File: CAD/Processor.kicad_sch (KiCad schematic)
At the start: 78 parts, among them M1 FID, M11 MOUNTING, M12 Logo_KICAD, M15 MOUNTING, M2 FID, M3 MOUNTING, M9 MOUNTING, U11 ATSAME70Q20B-ANT, X1 ECS-120-10-33B-CKM-TR

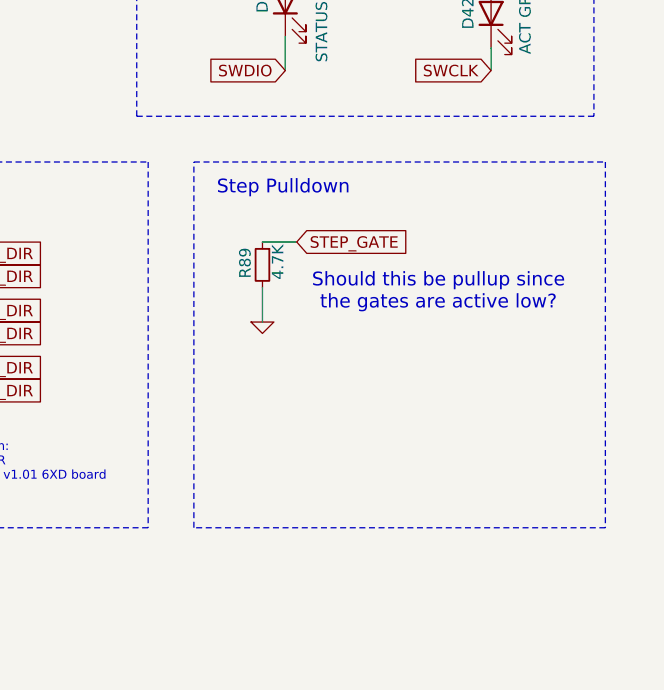
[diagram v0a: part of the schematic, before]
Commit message: Remove Step gate
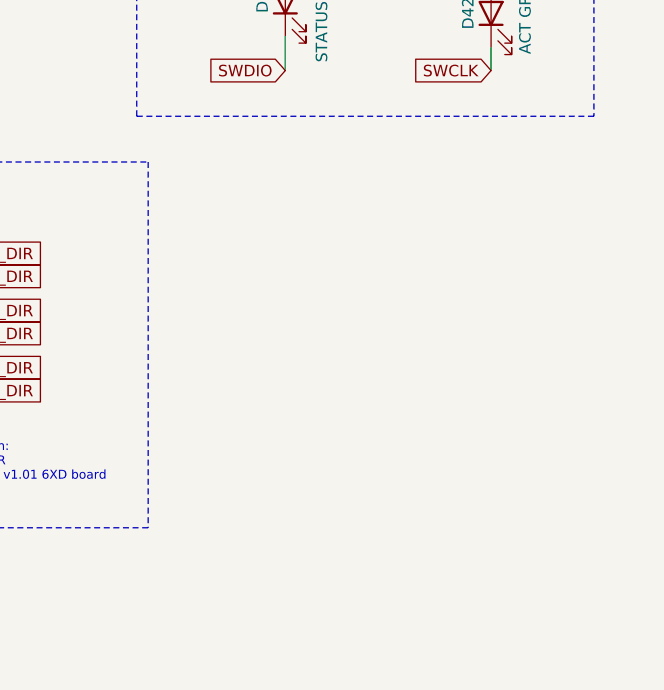
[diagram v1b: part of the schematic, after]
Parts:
- removed R89: 4.7K, Resistor_SMD:R_0402_1005Metric_Wbry, symbol Device:R_Small
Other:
- note removed: "Should this be pullup since the gates are active low?"
- note removed: "Step Pulldown"

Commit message: Pin Changes / Misc
Changing some pins around so I have a chip select
Processor Pins:
PC28 ---> PA9 (Driver_2_Step)
PC29[AFE1_AD4] ---> PB1[AFE1_AD0] (TEMP_1)
PC28 -> spi1cs1
PC29 -> spi1cs2 (Unused as of now)
IDC Header:
CAN 0 Lines removed
13 -> SPI1_MOSI_BUFF
14 -> SP1_MISO
18 -> SPI1_SPCK_BUFF
19 -> spi1cs1
Misc:
Fixed all library links, should get a lot less errors now
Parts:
- C150, C151, C152, C153, C154, C155, C157, C159, C160, C162, C163, C164, C165, C166, C167, C168, C62, C64, C66: footprint Capacitor_SMD:C_0402_1005Metric_Wbry -> Capacitor_SMD:C_0402_1005Metric
- C156, C161, C169, C200, C51, C55, C63, C65: footprint Capacitor_SMD:C_0603_1608Metric_Wbry -> Capacitor_SMD:C_0603_1608Metric
- D20: footprint complib:SOD-523F -> Diode_SMD:D_SOD-523
- L5, L6, L7, L8, R114, R28, R34, R35: footprint Resistor_SMD:R_0603_1608Metric_Wbry -> Resistor_SMD:R_0603_1608Metric
- M11, M15, M3, M9: footprint Carters_Various_Bits_and_Pieces:Fixing_M4 -> 3DPotter:Fixing_M4
- R111, R112, R113, R168, R175, R176, R177, R178, R21, R27, R29, R30, R31, R32, R33, R68, R9: footprint Resistor_SMD:R_0402_1005Metric_Wbry -> Resistor_SMD:R_0402_1005Metric
- TM1: footprint Carters_Various_Bits_and_Pieces:3DPotter Logo -> 3DPotter:3DPotter Logo
- X1: footprint complib:Crystal_SMD_ECS-33B-4Pin_3.2x2.5mm -> Crystal:Crystal_SMD_3225-4Pin_3.2x2.5mm
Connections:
- net DRIVER_2_STEP: now also U11.75 (PA9); no longer U11.76 (PC28)
- net TEMP_1: now also U11.20 (PB1); no longer U11.16 (PC29)
- new net spi1cs1: U11.76 (PC28)
- new net spi1cs2: U11.16 (PC29)
- no-connect marks 33 -> 31
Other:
- note added: "CS0 controls both SBC and ESP_WIFI, you can only use one or the other, as plugging in an SBC takes over networking"
- note added: "CS1 is for daughter boards that are connected through the IDC header CS2 is unused for now, I can't think of anything that would need it."

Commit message: Board Finished
Board has been slightly modified to add SPI to the BBC.
A lot of library mismatch/ not found errors were fixed. Only errors that exist currently are all related to the silkscreen edges on all 0402 components.
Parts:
- removed M12: Logo_KICAD, Symbol:KiCad-Logo_6mm_SilkScreen, symbol Duet3:Logo_KICAD
- TM1: footprint 3DPotter:3DPotter Logo -> 3DPotter:3DPotter Logo 10x10mm
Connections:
- net IO_0_O: now reaches R168.1, U11.53 (PD26)
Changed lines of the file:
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@@
 		)
 	)
+	(label "IO_0_O"
+		(at 175.26 213.36 0)
+		(effects
+			(font
+				(size 1.27 1.27)
+			)
+			(justify left bottom)
+		)
+	)
 	(label "VDDPLL"
 		(at 152.4 50.8 90)
@@
 	)
 	(symbol
-		(lib_id "Duet3:Logo_KICAD")
-		(at 132.715 397.51 0)
-		(unit 1)
-		(exclude_from_sim no)
-		(in_bom no)
-		(on_board yes)
-		(dnp no)
-		(property "Reference" "M12"
-			(at 136.652 396.2146 0)
-			(effects
-				(font
-					(size 1.524 1.524)
-				)
-				(justify left)
-				(hide yes)
-			)
-		)
-		(property "Value" "Logo_KICAD"
-			(at 136.652 397.5608 0)
-			(effects
-				(font
-					(size 1.524 1.524)
-				)
-				(justify left)
-				(hide yes)
-			)
-		)
-		(property "Footprint" "Symbol:KiCad-Logo_6mm_SilkScreen"
-			(at 136.652 397.5608 0)
-			(effects
-				(font
-					(size 1.524 1.524)
-				)
-				(justify left)
-				(hide yes)
-			)
-		)
-		(property "Datasheet" ""
-			(at 132.715 397.51 0)
-			(effects
-				(font
-					(size 1.524 1.524)
-				)
-			)
-		)
-		(property "Description" ""
-			(at 132.715 397.51 0)
-			(effects
-				(font
-					(size 1.27 1.27)
-				)
-				(hide yes)
-			)
-		)
-		(property "Part Number" "Virtual Component DNP"
-			(at 132.715 397.51 0)
-			(effects
-				(font
-					(size 1.27 1.27)
-				)
-				(hide yes)
-			)
-		)
-		(instances
-			(project ""
-				(path "/94813053-1316-4754-9fb4-4dbbf7dc780d/00000000-0000-0000-0000-000050523307"
-					(reference "M12")
-					(unit 1)
-				)
-			)
-		)
-	)
-	(symbol
 		(lib_id "Device:R_Small")
 		(at 241.3 52.07 270)
@@
 			)
 		)
-		(property "Footprint" "3DPotter:3DPotter Logo"
+		(property "Footprint" "3DPotter:3DPotter Logo 10x10mm"
 			(at 140.97 396.24 0)
 			(effects

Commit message: move driver 2 step to be on the same port as the others
this is moderately important (not critical, but better for software reasons)
also I added the silkscreen issues to 'ignore'
also routed the pin change
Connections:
- net DRIVER_2_STEP: now also U11.127 (PC23); no longer U11.75 (PA9)
- no-connect marks 31 -> 30
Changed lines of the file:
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@@
 	)
 	(no_connect
-		(at 175.26 121.92)
-	)
-	(no_connect
 		(at 175.26 187.96)
 	)
@@
 	(wire
 		(pts
-			(xy 109.22 86.36) (xy 114.3 86.36)
-		)
-		(stroke
-			(width 0)
-			(type default)
-		)
-	)
-	(wire
-		(pts
 			(xy 154.94 24.13) (xy 154.94 25.4)
 		)
@@
 	(wire
 		(pts
+			(xy 175.26 121.92) (xy 180.3918 121.92)
+		)
+		(stroke
+			(width 0)
+			(type default)
+		)
+	)
+	(wire
+		(pts
 			(xy 121.92 38.1) (xy 121.92 21.59)
 		)
@@
 		)
 	)
-	(global_label "DRIVER_2_STEP"
-		(shape input)
-		(at 109.22 86.36 180)
-		(fields_autoplaced yes)
-		(effects
-			(font
-				(size 1.27 1.27)
-			)
-			(justify right)
-		)
-		(property "Intersheetrefs" "${INTERSHEET_REFS}"
-			(at 92.4958 86.36 0)
-			(effects
-				(font
-					(size 1.27 1.27)
-				)
-				(justify right)
-				(hide yes)
-			)
-		)
-	)
 	(global_label "DRIVER_3_DIR"
 		(shape input)
@@
 				(hide yes)
 			)
+		)
+	)
+	(global_label "DRIVER_2_STEP"
+		(shape input)
+		(at 180.3918 121.92 0)
+		(fields_autoplaced yes)
+		(effects
+			(font
+				(size 1.27 1.27)
+			)
+			(justify left)
+		)
+		(property "Intersheetrefs" "${INTERSHEET_REFS}"
+			(at 197.116 121.92 0)
+			(effects
+				(font
+					(size 1.27 1.27)
+				)
+				(justify left)
+				(hide yes)
+			)
